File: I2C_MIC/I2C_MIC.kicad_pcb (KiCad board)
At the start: 2 copper layers, 18.7 x 16.5 mm, 9 parts, among them J1 I2S_PMOD

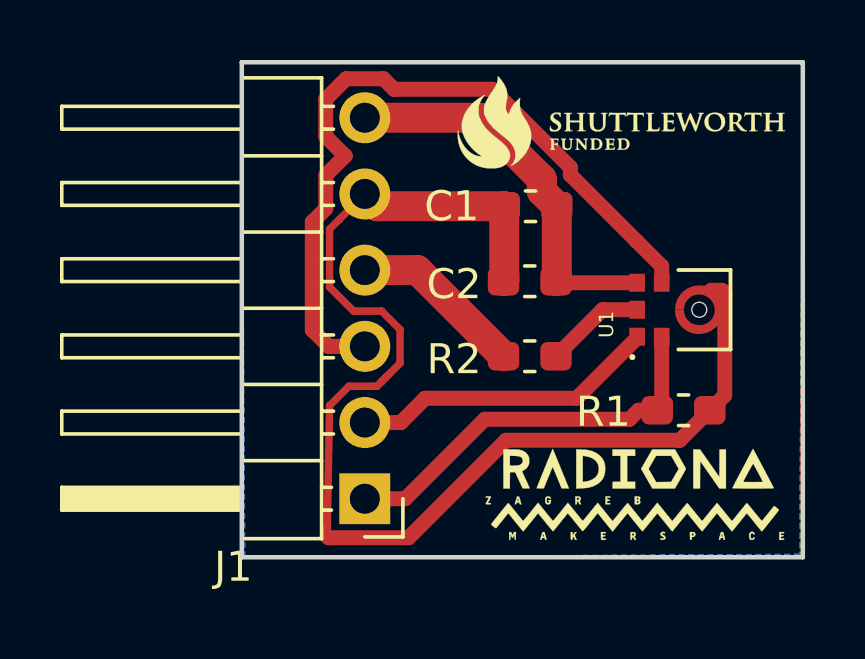
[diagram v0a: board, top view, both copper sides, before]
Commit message: Fixing I2S-MIC
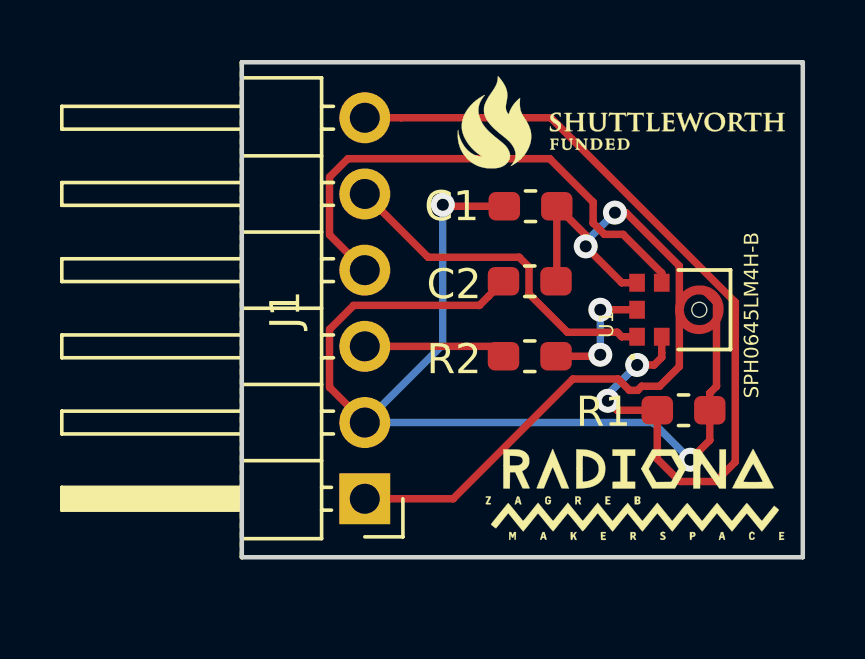
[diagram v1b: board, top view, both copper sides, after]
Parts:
- U1: value (none) -> SPH0645LM4H-B
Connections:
- J1 pad 1: SELECT -> 3V3
- J1 pad 2: WS -> GND
- J1 pad 3: BCLK -> DOUT
- J1 pad 4: DOUT -> BCLK
- J1 pad 5: GND -> WS
- J1 pad 6: 3V3 -> SELECT
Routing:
- net SELECT: track 13.5 -> 30.0 mm, vias 0 -> 2
- net 3V3: track 17.0 -> 26.9 mm, vias 0 -> 2
- net BCLK: track 25.2 -> 17.2 mm
- net GND: track 41.9 -> 38.2 mm, vias 0 -> 2
- net WS: track 10.3 -> 11.6 mm
- net DOUT: track 5.81 -> 4.76 mm
- net DOUT_MIC: track 3.34 -> 4.22 mm, vias 0 -> 2

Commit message: New versions
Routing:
- net 3V3: track 26.9 -> 36.4 mm, vias 2 -> 4
- net SELECT: track 30.0 -> 33.0 mm
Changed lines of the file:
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@@
     (thickness 1.6)
     (drawings 10)
-    (tracks 87)
+    (tracks 89)
     (zones 0)
     (modules 9)
@@
       (layerselection 0x010fc_ffffffff)
       (usegerberextensions false)
-      (usegerberattributes false)
-      (usegerberadvancedattributes false)
+      (usegerberattributes true)
+      (usegerberadvancedattributes true)
       (creategerberjobfile false)
       (excludeedgelayer true)
@@
       (outputformat 1)
       (mirror false)
-      (drillshape 1)
+      (drillshape 0)
       (scaleselection 1)
-      (outputdirectory ""))
+      (outputdirectory "Gerber/"))
   )
   (net 0 "")
@@
   (segment (start 163.763747 84.263747) (end 163.763747 84.637389) (width 0.25) (layer F.Cu) (net 1))
   (segment (start 162.8 83.3) (end 163.763747 84.263747) (width 0.25) (layer F.Cu) (net 1))
-  (segment (start 166.225001 89.29999) (end 166.884001 88.64099) (width 0.25) (layer F.Cu) (net 1))
+  (segment (start 166.884001 85.289999) (end 165.106662 83.51266) (width 0.25) (layer F.Cu) (net 1))
   (segment (start 156.4 93.05) (end 159.34551 93.05) (width 0.25) (layer F.Cu) (net 1))
-  (segment (start 163.335521 89.059989) (end 164.848001 89.059989) (width 0.25) (layer F.Cu) (net 1))
-  (segment (start 165.492501 89.436989) (end 165.6295 89.29999) (width 0.25) (layer F.Cu) (net 1))
-  (segment (start 165.6295 89.29999) (end 166.225001 89.29999) (width 0.25) (layer F.Cu) (net 1))
-  (segment (start 166.884001 85.289999) (end 165.106662 83.51266) (width 0.25) (layer F.Cu) (net 1))
-  (segment (start 164.848001 89.059989) (end 165.225001 89.436989) (width 0.25) (layer F.Cu) (net 1))
   (segment (start 165.106662 83.51266) (end 164.73734 83.51266) (width 0.25) (layer F.Cu) (net 1))
-  (segment (start 165.225001 89.436989) (end 165.492501 89.436989) (width 0.25) (layer F.Cu) (net 1))
-  (segment (start 166.884001 88.64099) (end 166.884001 85.289999) (width 0.25) (layer F.Cu) (net 1))
-  (segment (start 159.34551 93.05) (end 163.335521 89.059989) (width 0.25) (layer F.Cu) (net 1))
+  (via (at 168.5 85.25) (size 0.8) (drill 0.4) (layers F.Cu B.Cu) (net 1))
+  (segment (start 168.460001 85.289999) (end 168.5 85.25) (width 0.25) (layer F.Cu) (net 1))
+  (segment (start 166.884001 85.289999) (end 168.460001 85.289999) (width 0.25) (layer F.Cu) (net 1))
+  (via (at 169.25 93) (size 0.8) (drill 0.4) (layers F.Cu B.Cu) (net 1))
+  (segment (start 169.25 86) (end 169.25 93) (width 0.25) (layer B.Cu) (net 1))
+  (segment (start 168.5 85.25) (end 169.25 86) (width 0.25) (layer B.Cu) (net 1))
+  (segment (start 156.45 93) (end 156.4 93.05) (width 0.25) (layer F.Cu) (net 1))
+  (segment (start 169.25 93) (end 156.45 93) (width 0.25) (layer F.Cu) (net 1))
   (segment (start 160.525928 86.299072) (end 161.025 85.8) (width 0.25) (layer F.Cu) (net 2))
   (segment (start 160.219999 86.605001) (end 160.525928 86.299072) (width 0.25) (layer F.Cu) (net 2))
@@
   (segment (start 156.4 90.51) (end 155.224999 89.334999) (width 0.25) (layer F.Cu) (net 2))
   (segment (start 167.9 90.1) (end 167.9 89.525) (width 0.25) (layer F.Cu) (net 2))
-  (segment (start 168.125001 89.299999) (end 168.125001 86.511411) (width 0.25) (layer F.Cu) (net 2))
   (segment (start 168.125001 86.511411) (end 167.71359 86.1) (width 0.25) (layer F.Cu) (net 2))
   (segment (start 167.71359 86.1) (end 167.53 86.1) (width 0.25) (layer F.Cu) (net 2))
@@
   (segment (start 166.01 90.51) (end 156.4 90.51) (width 0.25) (layer B.Cu) (net 2))
   (segment (start 167.25 91.75) (end 166.01 90.51) (width 0.25) (layer B.Cu) (net 2))
+  (segment (start 168.125001 88.5) (end 168.125001 86.511411) (width 0.25) (layer F.Cu) (net 2))
+  (segment (start 168.125001 89.299999) (end 168.125001 88.5) (width 0.25) (layer F.Cu) (net 2))
   (via (at 165.479071 88.590754) (size 0.8) (drill 0.4) (layers F.Cu B.Cu) (net 3))
   (segment (start 166.298 88.2) (end 166.298 87.65) (width 0.25) (layer F.Cu) (net 3))
@@
   (segment (start 166.044756 88.590754) (end 166.298 88.33751) (width 0.25) (layer F.Cu) (net 3))
   (segment (start 165.479071 88.590754) (end 166.044756 88.590754) (width 0.25) (layer F.Cu) (net 3))
-  (segment (start 166.15 90.1) (end 166.15 91.723004) (width 0.25) (layer F.Cu) (net 3))
-  (segment (start 168.75001 86.50001) (end 162.6 80.35) (width 0.25) (layer F.Cu) (net 3))
-  (segment (start 162.6 80.35) (end 157.602081 80.35) (width 0.25) (layer F.Cu) (net 3))
-  (segment (start 168.75001 91.822994) (end 168.75001 86.50001) (width 0.25) (layer F.Cu) (net 3))
-  (segment (start 166.901998 92.475002) (end 168.098002 92.475002) (width 0.25) (layer F.Cu) (net 3))
-  (segment (start 157.602081 80.35) (end 156.4 80.35) (width 0.25) (layer F.Cu) (net 3))
-  (segment (start 166.15 91.723004) (end 166.901998 92.475002) (width 0.25) (layer F.Cu) (net 3))
-  (segment (start 168.098002 92.475002) (end 168.75001 91.822994) (width 0.25) (layer F.Cu) (net 3))
   (via (at 164.5 89.78499) (size 0.8) (drill 0.4) (layers F.Cu B.Cu) (net 3))
   (segment (start 165.479071 88.590754) (end 164.5 89.569825) (width 0.25) (layer B.Cu) (net 3))
@@
   (segment (start 164.5 89.569825) (end 164.5 89.78499) (width 0.25) (layer B.Cu) (net 3))
   (segment (start 164.81501 90.1) (end 164.5 89.78499) (width 0.25) (layer F.Cu) (net 3))
+  (segment (start 169.450011 90.913578) (end 169.450011 84.563601) (width 0.25) (layer F.Cu) (net 3))
+  (segment (start 169.450011 84.563601) (end 165.23641 80.35) (width 0.25) (layer F.Cu) (net 3))
+  (segment (start 167.8136 92.549989) (end 169.450011 90.913578) (width 0.25) (layer F.Cu) (net 3))
+  (segment (start 165.23641 80.35) (end 157.602081 80.35) (width 0.25) (layer F.Cu) (net 3))
+  (segment (start 166.15 90.1) (end 165.650928 90.599072) (width 0.25) (layer F.Cu) (net 3))
+  (segment (start 157.602081 80.35) (end 156.4 80.35) (width 0.25) (layer F.Cu) (net 3))
+  (segment (start 166.15 92.549989) (end 167.8136 92.549989) (width 0.25) (layer F.Cu) (net 3))
+  (segment (start 165.650928 92.050917) (end 166.15 92.549989) (width 0.25) (layer F.Cu) (net 3))
+  (segment (start 165.650928 90.599072) (end 165.650928 92.050917) (width 0.25) (layer F.Cu) (net 3))
   (segment (start 163.15448 87.49999) (end 164.81499 87.49999) (width 0.25) (layer F.Cu) (net 4))
   (segment (start 164.965 87.65) (end 165.476 87.65) (width 0.25) (layer F.Cu) (net 4))
